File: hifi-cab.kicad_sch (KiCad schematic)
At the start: 30 parts, among them J1 IR, J2 FAN 1, J3 FAN 2, J4 FAN 3, J5 DS18B20, J6 PWR IN, J7 RS-232, Q1 AO3400A, Q2 AO3400A, Q3 AO3400A, Q4 AO3400A, U1 TSR0.5-2433, U2 esp32-wemos-d1-mini

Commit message: Power routing complete
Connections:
- net +3.3V: now also J1.1 (Pin_1); no longer J1.2 (Pin_2)
- net RX: now also J7.2 (Pin_2); no longer J7.3 (Pin_3)
- net TX: now also J7.3 (Pin_3); no longer J7.2 (Pin_2)
- net at R9.1: now also J1.2 (Pin_2); no longer J1.1 (Pin_1)
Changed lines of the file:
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@@
 	(wire
 		(pts
+			(xy 85.09 162.56) (xy 85.09 158.75)
+		)
+		(stroke
+			(width 0)
+			(type default)
+		)
+	)
+	(wire
+		(pts
 			(xy 73.66 97.79) (xy 73.66 99.06)
 		)
@@
 	(wire
 		(pts
-			(xy 76.2 165.1) (xy 85.09 165.1)
-		)
-		(stroke
-			(width 0)
-			(type default)
-		)
-	)
-	(wire
-		(pts
 			(xy 93.98 92.71) (xy 93.98 107.95)
 		)
@@
 	(wire
 		(pts
-			(xy 76.2 162.56) (xy 86.36 162.56)
-		)
-		(stroke
-			(width 0)
-			(type default)
-		)
-	)
-	(wire
-		(pts
 			(xy 114.3 27.94) (xy 114.3 38.1)
 		)
@@
 	(wire
 		(pts
-			(xy 38.1 162.56) (xy 40.64 162.56)
+			(xy 76.2 162.56) (xy 85.09 162.56)
 		)
 		(stroke
@@
 	(wire
 		(pts
-			(xy 138.43 162.56) (xy 134.62 162.56)
+			(xy 38.1 162.56) (xy 40.64 162.56)
 		)
 		(stroke
@@
 	(wire
 		(pts
-			(xy 29.21 172.72) (xy 29.21 173.99)
+			(xy 138.43 162.56) (xy 134.62 162.56)
 		)
 		(stroke
@@
 	(wire
 		(pts
-			(xy 240.03 129.54) (xy 240.03 120.65)
+			(xy 29.21 172.72) (xy 29.21 173.99)
 		)
 		(stroke
@@
 	(wire
 		(pts
-			(xy 114.3 38.1) (xy 114.3 39.37)
+			(xy 240.03 129.54) (xy 240.03 120.65)
 		)
 		(stroke
@@
 	(wire
 		(pts
-			(xy 85.09 165.1) (xy 85.09 158.75)
+			(xy 114.3 38.1) (xy 114.3 39.37)
 		)
 		(stroke
@@
 	(wire
 		(pts
+			(xy 76.2 165.1) (xy 86.36 165.1)
+		)
+		(stroke
+			(width 0)
+			(type default)
+		)
+	)
+	(wire
+		(pts
 			(xy 53.34 66.04) (xy 53.34 69.85)
 		)
@@
 	(wire
 		(pts
-			(xy 85.09 46.99) (xy 85.09 48.26)
+			(xy 96.52 165.1) (xy 93.98 165.1)
 		)
 		(stroke
@@
 	(wire
 		(pts
-			(xy 96.52 162.56) (xy 93.98 162.56)
+			(xy 85.09 46.99) (xy 85.09 48.26)
 		)
 		(stroke
@@
 		)
 	)
+	(global_label "RX"
+		(shape input)
+		(at 243.84 134.62 180)
+		(fields_autoplaced yes)
+		(effects
+			(font
+				(size 1.27 1.27)
+			)
+			(justify right)
+		)
+		(property "Intersheetrefs" "${INTERSHEET_REFS}"
+			(at 238.3753 134.62 0)
+			(hide yes)
+			(show_name no)
+			(do_not_autoplace no)
+			(effects
+				(font
+					(size 1.27 1.27)
+				)
+				(justify right)
+			)
+		)
+	)
+	(global_label "IR_1"
+		(shape input)
+		(at 96.52 165.1 0)
+		(fields_autoplaced yes)
+		(effects
+			(font
+				(size 1.27 1.27)
+			)
+			(justify left)
+		)
+		(property "Intersheetrefs" "${INTERSHEET_REFS}"
+			(at 103.5571 165.1 0)
+			(hide yes)
+			(show_name no)
+			(do_not_autoplace no)
+			(effects
+				(font
+					(size 1.27 1.27)
+				)
+				(justify left)
+			)
+		)
+	)
 	(global_label "RPM1"
 		(shape input)
@@
 		)
 	)
+	(global_label "TX"
+		(shape input)
+		(at 243.84 132.08 180)
+		(fields_autoplaced yes)
+		(effects
+			(font
+				(size 1.27 1.27)
+			)
+			(justify right)
+		)
+		(property "Intersheetrefs" "${INTERSHEET_REFS}"
+			(at 238.6777 132.08 0)
+			(hide yes)
+			(show_name no)
+			(do_not_autoplace no)
+			(effects
+				(font
+					(size 1.27 1.27)
+				)
+				(justify right)
+			)
+		)
+	)
 	(global_label "FAN2"
 		(shape input)
@@
 		)
 	)
-	(global_label "IR_1"
-		(shape input)
-		(at 96.52 162.56 0)
-		(fields_autoplaced yes)
-		(effects
-			(font
-				(size 1.27 1.27)
-			)
-			(justify left)
-		)
-		(property "Intersheetrefs" "${INTERSHEET_REFS}"
-			(at 103.5571 162.56 0)
-			(hide yes)
-			(show_name no)
-			(do_not_autoplace no)
-			(effects
-				(font
-					(size 1.27 1.27)
-				)
-				(justify left)
-			)
-		)
-	)
 	(global_label "TACH1"
 		(shape input)
@@
 		)
 	)
-	(global_label "TX"
-		(shape input)
-		(at 243.84 134.62 180)
-		(fields_autoplaced yes)
-		(effects
-			(font
-				(size 1.27 1.27)
-			)
-			(justify right)
-		)
-		(property "Intersheetrefs" "${INTERSHEET_REFS}"
-			(at 238.6777 134.62 0)
-			(hide yes)
-			(show_name no)
-			(do_not_autoplace no)
-			(effects
-				(font
-					(size 1.27 1.27)
-				)
-				(justify right)
-			)
-		)
-	)
 	(global_label "IR_C"
 		(shape input)
@@
 		)
 	)
-	(global_label "RX"
-		(shape input)
-		(at 243.84 132.08 180)
-		(fields_autoplaced yes)
-		(effects
-			(font
-				(size 1.27 1.27)
-			)
-			(justify right)
-		)
-		(property "Intersheetrefs" "${INTERSHEET_REFS}"
-			(at 238.3753 132.08 0)
-			(hide yes)
-			(show_name no)
-			(do_not_autoplace no)
-			(effects
-				(font
-					(size 1.27 1.27)
-				)
-				(justify right)
-			)
-		)
-	)
 	(global_label "RPM2"
 		(shape input)
@@
 	)
 	(symbol
-		(lib_id "Device:R")
-		(at 90.17 162.56 90)
-		(unit 1)
-		(body_style 1)
-		(exclude_from_sim no)
-		(in_bom yes)
-		(on_board yes)
-		(in_pos_files yes)
-		(dnp no)
-		(property "Reference" "R9"
-			(at 90.17 157.48 90)
-			(show_name no)
-			(do_not_autoplace no)
-			(effects
-				(font
-					(size 1.27 1.27)
-				)
-			)
-		)
-		(property "Value" "68R"
-			(at 90.17 159.766 90)
-			(show_name no)
-			(do_not_autoplace no)
-			(effects
-				(font
-					(size 1.27 1.27)
-				)
-			)
-		)
-		(property "Footprint" "Resistor_THT:R_Axial_DIN0204_L3.6mm_D1.6mm_P5.08mm_Horizontal"
-			(at 90.17 164.338 90)
-			(hide yes)
-			(show_name no)
-			(do_not_autoplace no)
-			(effects
-				(font
-					(size 1.27 1.27)
-				)
-			)
-		)
-		(property "Datasheet" ""
-			(at 90.17 162.56 0)
-			(hide yes)
-			(show_name no)
-			(do_not_autoplace no)
-			(effects
-				(font
-					(size 1.27 1.27)
-				)
-			)
-		)
-		(property "Description" "Resistor"
-			(at 90.17 162.56 0)
-			(hide yes)
-			(show_name no)
-			(do_not_autoplace no)
-			(effects
-				(font
-					(size 1.27 1.27)
-				)
-			)
-		)
-		(pin "1"
-		)
-		(pin "2"
-		)
-		(instances
-			(project "hifi-cab"
-				(path "/464ef4ad-8e38-4b55-beb7-b05b4d6675da"
-					(reference "R9")
-					(unit 1)
-				)
-			)
-		)
-	)
-	(symbol
 		(lib_id "Transistor_FET:AO3400A")
 		(at 50.8 74.93 0)
@@
 					(unit 1)
 				)
+			)
+		)
+	)
+	(symbol
+		(lib_id "Device:R")
+		(at 90.17 165.1 90)
+		(unit 1)
+		(body_style 1)
+		(exclude_from_sim no)
+		(in_bom yes)
+		(on_board yes)
+		(in_pos_files yes)
+		(dnp no)
+		(property "Reference" "R9"
+			(at 90.17 160.02 90)
+			(show_name no)
+			(do_not_autoplace no)
+			(effects
+				(font
+					(size 1.27 1.27)
+				)
+			)
+		)
+		(property "Value" "68R"
+			(at 90.17 162.306 90)
+			(show_name no)
+			(do_not_autoplace no)
+			(effects
+				(font
+					(size 1.27 1.27)
+				)
+			)
+		)
+		(property "Footprint" "Resistor_THT:R_Axial_DIN0204_L3.6mm_D1.6mm_P5.08mm_Horizontal"
+			(at 90.17 166.878 90)
+			(hide yes)
+			(show_name no)
+			(do_not_autoplace no)
+			(effects
+				(font
+					(size 1.27 1.27)
+				)
+			)
+		)
+		(property "Datasheet" ""
+			(at 90.17 165.1 0)
+			(hide yes)
+			(show_name no)
+			(do_not_autoplace no)
+			(effects
+				(font
+					(size 1.27 1.27)
+				)
+			)
+		)
+		(property "Description" "Resistor"
+			(at 90.17 165.1 0)
+			(hide yes)
+			(show_name no)
+			(do_not_autoplace no)
+			(effects
+				(font
+					(size 1.27 1.27)
+				)
+			)
+		)
+		(pin "1"
+		)
+		(pin "2"
+		)
+		(instances
+			(project "hifi-cab"
+				(path "/464ef4ad-8e38-4b55-beb7-b05b4d6675da"
+					(reference "R9")
+					(unit 1)
+				)

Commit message: Start DRC
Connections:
- net DS18B20: now also U2.4 (IO_36/SVP/A0); no longer U2.11 (IO_34)
- net FAN1_C: now also U2.6 (IO_26/D0); no longer U2.29 (IO_17/D3)
- net FAN3_C: now also U2.10 (IO_19/D6); no longer U2.7 (IO_35)
- net IR_C: now also U2.12 (IO_23/D7); no longer U2.31 (IO_16/D4)
- net RPM1: now also U2.13 (IO_14/TMS); no longer U2.27 (IO_21/D2/SDA)
- net RPM2: now also U2.9 (IO_33); no longer U2.25 (IO_22/D1/SCL)
- net RPM3: now also U2.7 (IO_35); no longer U2.12 (IO_23/D7)
- net TACH1: now also U2.18 (IO_13/TCK); no longer U2.26 (IO_25)
- net TACH2: now also U2.11 (IO_34); no longer U2.6 (IO_26/D0)
- net TACH3: now also U2.5 (IO_39/SVN); no longer U2.24 (IO_27)

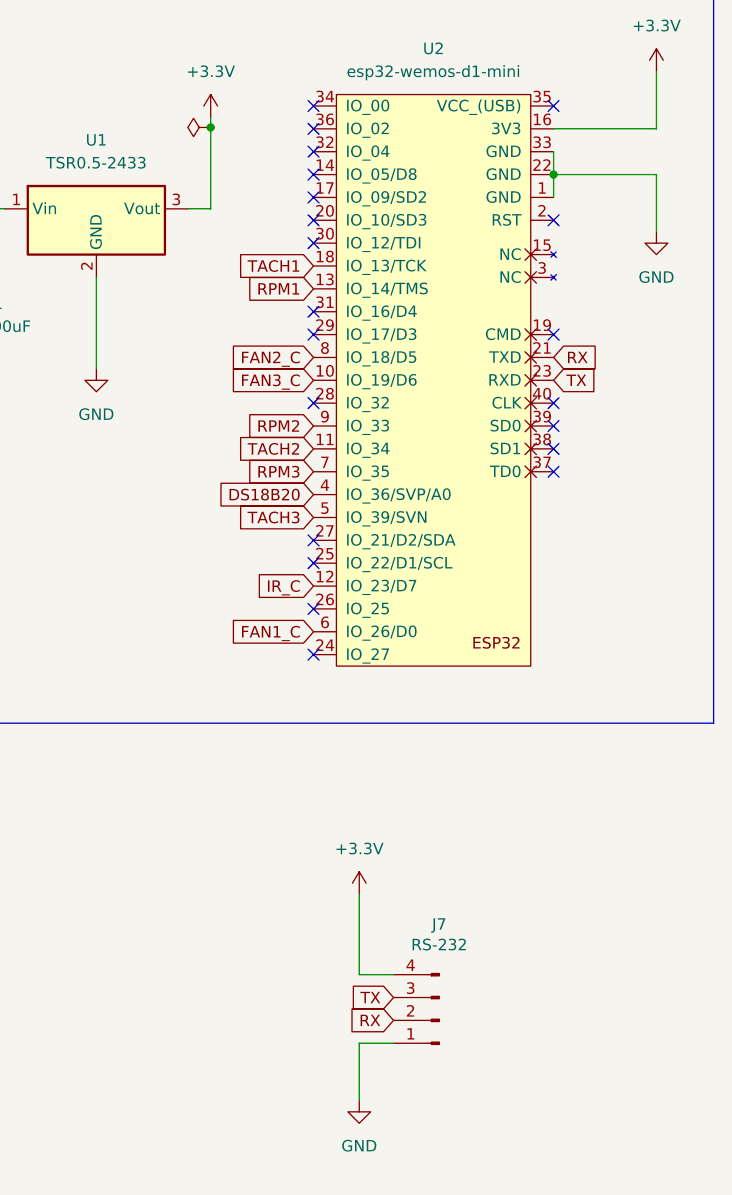
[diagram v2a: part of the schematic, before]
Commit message: Fix pin selection
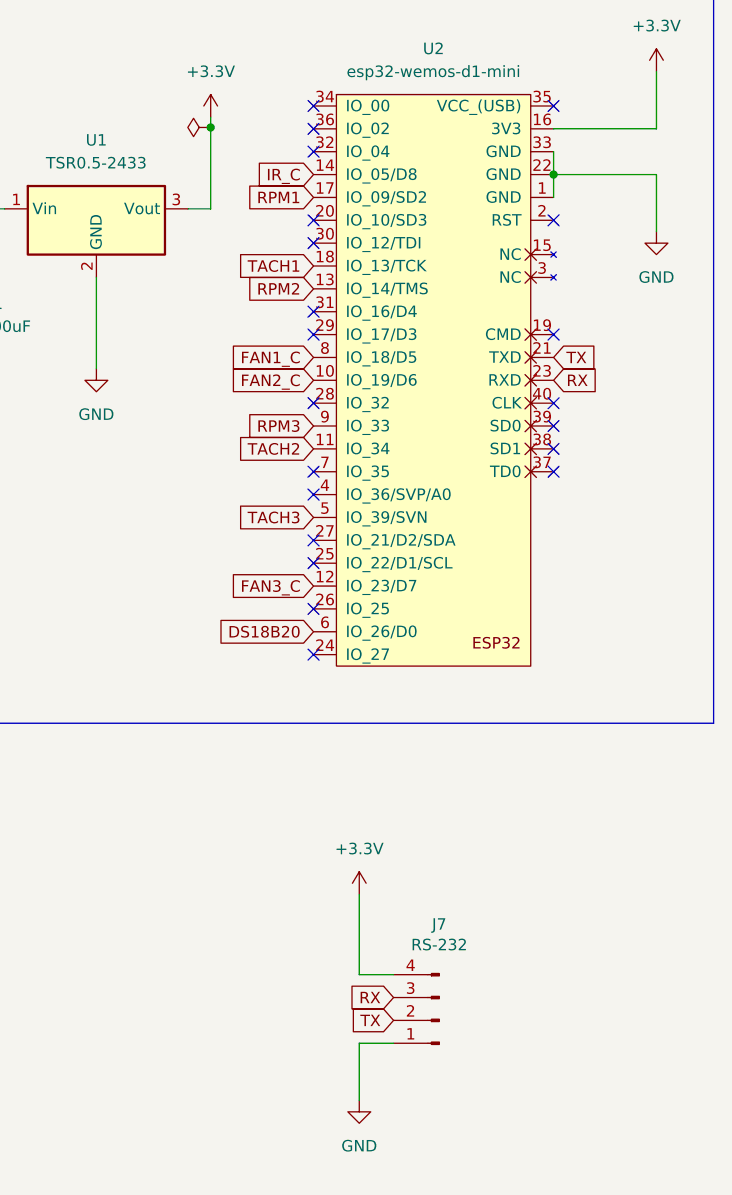
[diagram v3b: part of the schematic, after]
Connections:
- net DS18B20: now also U2.6 (IO_26/D0); no longer U2.4 (IO_36/SVP/A0)
- net FAN1_C: now also U2.8 (IO_18/D5); no longer U2.6 (IO_26/D0)
- net FAN2_C: now also U2.10 (IO_19/D6); no longer U2.8 (IO_18/D5)
- net FAN3_C: now also U2.12 (IO_23/D7); no longer U2.10 (IO_19/D6)
- net IR_C: now also U2.14 (IO_05/D8); no longer U2.12 (IO_23/D7)
- net RPM1: now also U2.17 (IO_09/SD2); no longer U2.13 (IO_14/TMS)
- net RPM2: now also U2.13 (IO_14/TMS); no longer U2.9 (IO_33)
- net RPM3: now also U2.9 (IO_33); no longer U2.7 (IO_35)
- net RX: now also J7.3 (Pin_3), U2.23 (RXD); no longer J7.2 (Pin_2), U2.21 (TXD)
- net TX: now also J7.2 (Pin_2), U2.21 (TXD); no longer J7.3 (Pin_3), U2.23 (RXD)

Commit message: Change C1 footprint
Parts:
- added C2: 100nF, Capacitor_SMD:C_0805_2012Metric_Pad1.18x1.45mm_HandSolder, symbol Device:C
- C1: footprint Capacitor_THT:CP_Radial_D5.0mm_P2.50mm -> Capacitor_THT:CP_Radial_D6.3mm_P2.50mm
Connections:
- net +3.3V: now also C2.1
- net at J1.2 (Pin_2), R9.1: now also C2.2
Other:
- moved on the sheet: R9
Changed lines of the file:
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@@
 	)
 	(junction
+		(at 85.09 162.56)
+		(diameter 0)
+		(color 0 0 0 0)
+	)
+	(junction
 		(at 86.36 106.68)
 		(diameter 0)
@@
 	)
 	(junction
+		(at 80.01 165.1)
+		(diameter 0)
+		(color 0 0 0 0)
+	)
+	(junction
 		(at 261.62 40.64)
 		(diameter 0)
@@
 	(wire
 		(pts
+			(xy 85.09 162.56) (xy 85.09 167.64)
+		)
+		(stroke
+			(width 0)
+			(type default)
+		)
+	)
+	(wire
+		(pts
 			(xy 132.08 63.5) (xy 137.16 63.5)
 		)
@@
 	(wire
 		(pts
+			(xy 85.09 177.8) (xy 85.09 175.26)
+		)
+		(stroke
+			(width 0)
+			(type default)
+		)
+	)
+	(wire
+		(pts
 			(xy 34.29 48.26) (xy 34.29 49.53)
 		)
@@
 	(wire
 		(pts
+			(xy 85.09 177.8) (xy 80.01 177.8)
+		)
+		(stroke
+			(width 0)
+			(type default)
+		)
+	)
+	(wire
+		(pts
 			(xy 261.62 40.64) (xy 261.62 43.18)
 		)
@@
 	(wire
 		(pts
+			(xy 80.01 177.8) (xy 80.01 165.1)
+		)
+		(stroke
+			(width 0)
+			(type default)
+		)
+	)
+	(wire
+		(pts
 			(xy 24.13 162.56) (xy 29.21 162.56)
 		)
@@
 	(wire
 		(pts
+			(xy 80.01 165.1) (xy 90.17 165.1)
+		)
+		(stroke
+			(width 0)
+			(type default)
+		)
+	)
+	(wire
+		(pts
 			(xy 210.82 52.07) (xy 210.82 62.23)
 		)
@@
 	(wire
 		(pts
-			(xy 76.2 165.1) (xy 86.36 165.1)
+			(xy 76.2 165.1) (xy 80.01 165.1)
 		)
 		(stroke
@@
 	(wire
 		(pts
-			(xy 96.52 165.1) (xy 93.98 165.1)
+			(xy 100.33 165.1) (xy 97.79 165.1)
 		)
 		(stroke
@@
 	(global_label "IR_1"
 		(shape input)
-		(at 96.52 165.1 0)
+		(at 100.33 165.1 0)
 		(fields_autoplaced yes)
 		(effects
@@
 		)
 		(property "Intersheetrefs" "${INTERSHEET_REFS}"
-			(at 103.5571 165.1 0)
+			(at 107.3671 165.1 0)
 			(hide yes)
 			(show_name no)
@@
 	)
 	(symbol
+		(lib_id "Device:C")
+		(at 85.09 171.45 0)
+		(unit 1)
+		(body_style 1)
+		(exclude_from_sim no)
+		(in_bom yes)
+		(on_board yes)
+		(in_pos_files yes)
+		(dnp no)
+		(fields_autoplaced yes)
+		(property "Reference" "C2"
+			(at 88.9 170.1799 0)
+			(show_name no)
+			(do_not_autoplace no)
+			(effects
+				(font
+					(size 1.27 1.27)
+				)
+				(justify left)
+			)
+		)
+		(property "Value" "100nF"
+			(at 88.9 172.7199 0)
+			(show_name no)
+			(do_not_autoplace no)
+			(effects
+				(font
+					(size 1.27 1.27)
+				)
+				(justify left)
+			)
+		)
+		(property "Footprint" "Capacitor_SMD:C_0805_2012Metric_Pad1.18x1.45mm_HandSolder"
+			(at 86.0552 175.26 0)
+			(hide yes)
+			(show_name no)
+			(do_not_autoplace no)
+			(effects
+				(font
+					(size 1.27 1.27)
+				)
+			)
+		)
+		(property "Datasheet" ""
+			(at 85.09 171.45 0)
+			(hide yes)
+			(show_name no)
+			(do_not_autoplace no)
+			(effects
+				(font
+					(size 1.27 1.27)
+				)
+			)
+		)
+		(property "Description" "Unpolarized capacitor"
+			(at 85.09 171.45 0)
+			(hide yes)
+			(show_name no)
+			(do_not_autoplace no)
+			(effects
+				(font
+					(size 1.27 1.27)
+				)
+			)
+		)
+		(pin "1"
+		)
+		(pin "2"
+		)
+		(instances
+			(project "hifi-cab"
+				(path "/464ef4ad-8e38-4b55-beb7-b05b4d6675da"
+					(reference "C2")
+					(unit 1)
+				)
+			)
+		)
+	)
+	(symbol
 		(lib_id "power:GND")
 		(at 48.26 173.99 0)
@@
 			)
 		)
-		(property "Footprint" "Capacitor_THT:CP_Radial_D5.0mm_P2.50mm"
+		(property "Footprint" "Capacitor_THT:CP_Radial_D6.3mm_P2.50mm"
 			(at 195.2752 60.96 0)
 			(hide yes)
@@
 	(symbol
 		(lib_id "Device:R")
-		(at 90.17 165.1 90)
+		(at 93.98 165.1 90)
 		(unit 1)
 		(body_style 1)
@@
 		(dnp no)
 		(property "Reference" "R9"
-			(at 90.17 160.02 90)
+			(at 93.98 160.02 90)
 			(show_name no)
 			(do_not_autoplace no)
@@
 		)
 		(property "Value" "68R"
-			(at 90.17 162.306 90)
+			(at 93.98 162.306 90)
 			(show_name no)
 			(do_not_autoplace no)
@@
 		)
 		(property "Footprint" "Resistor_THT:R_Axial_DIN0204_L3.6mm_D1.6mm_P5.08mm_Horizontal"
-			(at 90.17 166.878 90)
+			(at 93.98 166.878 90)
 			(hide yes)
 			(show_name no)
@@
 		)
 		(property "Datasheet" ""
-			(at 90.17 165.1 0)
+			(at 93.98 165.1 0)
 			(hide yes)
 			(show_name no)
@@
 		)
 		(property "Description" "Resistor"
-			(at 90.17 165.1 0)
+			(at 93.98 165.1 0)
 			(hide yes)
 			(show_name no)
